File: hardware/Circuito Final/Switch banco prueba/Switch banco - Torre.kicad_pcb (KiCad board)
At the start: 2 copper layers, 20 x 20 mm, 6 parts, among them J1 Conn_01x04_Socket, Q1_1 MMBT2222A

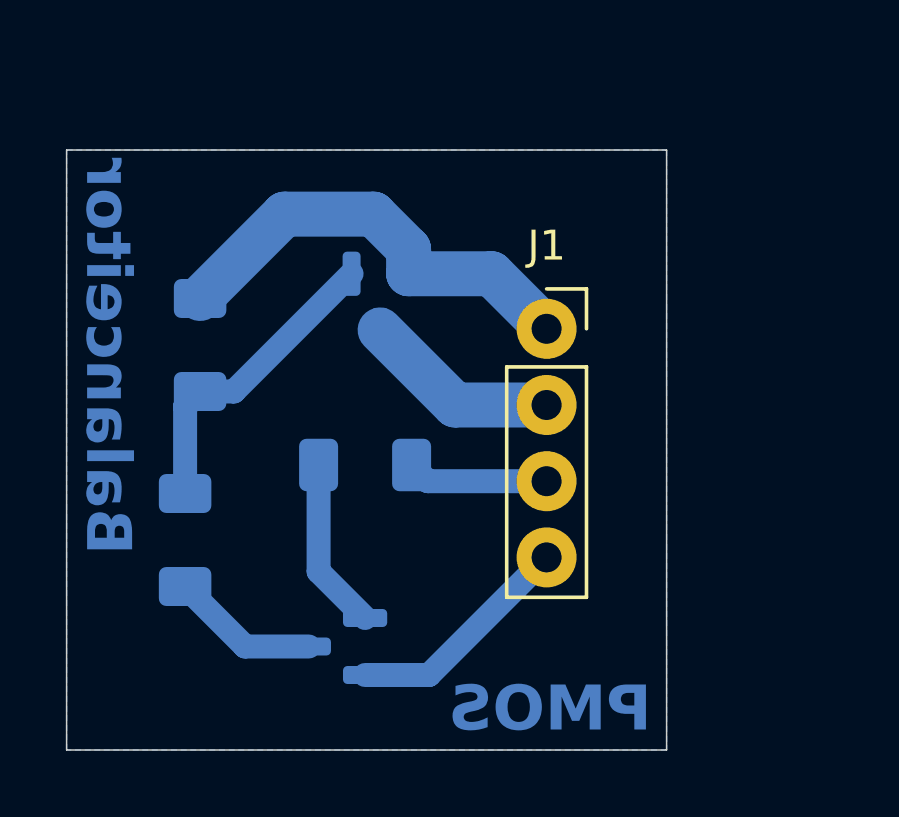
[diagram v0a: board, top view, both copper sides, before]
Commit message: update pcb celda y prueba del banco
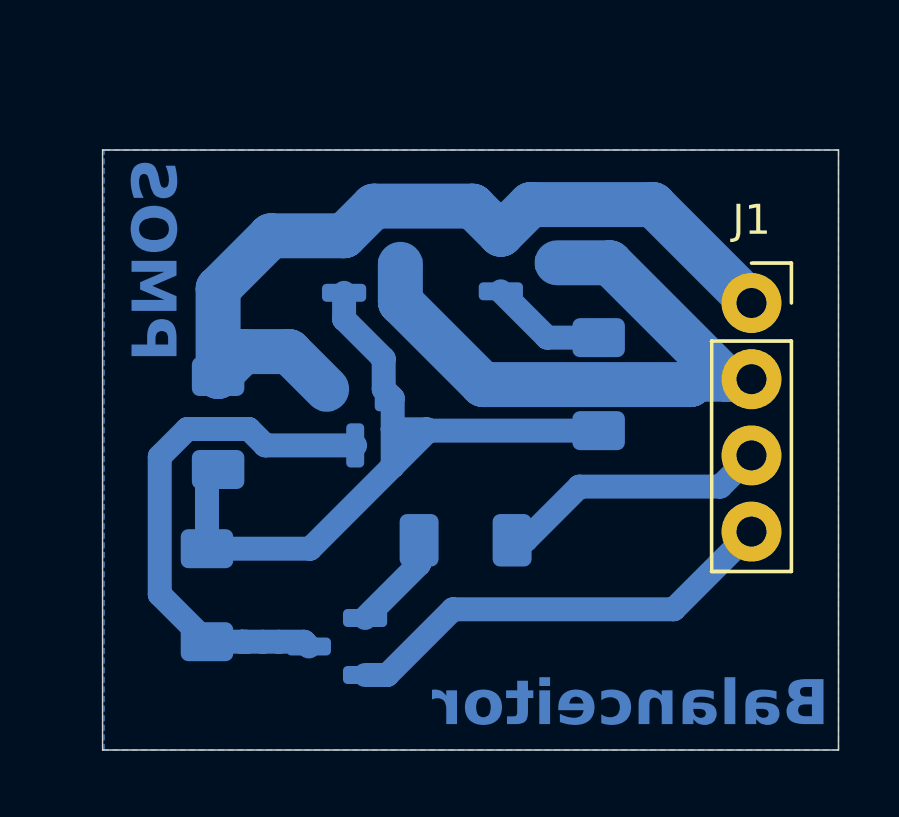
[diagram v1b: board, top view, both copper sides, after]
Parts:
- added Q1: MMBFJ112, Package_TO_SOT_SMD:SOT-23, B.Cu at (143.1, 102.9)
- added R1_10: 0, Resistor_SMD:R_1206_3216Metric_Pad1.30x1.75mm_HandSolder, B.Cu at (151.2, 101.8)
- added S2: IRLML6402, Package_TO_SOT_SMD:SOT-23, B.Cu at (143.7, 97.8)
- moved J1 6.88 mm to (156.3, 99.1)
- moved S1 5.13 mm to (148.9, 97.8), turned to 0 degrees
- moved R1_9 4.19 mm to (146.8, 107.0)
- moved R1_7 2.67 mm to (138.6, 103.1)
- moved R1_8 1.98 mm to (138.2, 108.8)
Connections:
- net Net-(S1-G) renamed /gate
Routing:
- net /gate: track 10.3 -> 29.0 mm
- net /bus_neg: track 6.59 -> 22.3 mm
- net /bus_pos: track 14.8 -> 28.5 mm
- net Net-(Q1-G): track 4.95 -> 17.6 mm
- net GND: track 7.67 -> 14.9 mm
- net /v_control: track 4.72 -> 9.15 mm
- net Net-(Q1_1-B): track 5.74 -> 3.34 mm
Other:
- board size 20 x 20 mm -> 24.5 x 20 mm
